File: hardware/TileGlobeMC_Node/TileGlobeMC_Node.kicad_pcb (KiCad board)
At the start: 2 copper layers, 85 x 40 mm, 164 parts, among them J1 P_Female, J10 LCD, J11 USB_C, J12 P_Female_Fallback, J13 P_Male_Fallback, J14 P_Female_Fallback, J15 P_Male_Fallback, J16 P_Female_Fallback, J17 P_Male_Fallback, J18 P_Female_Fallback, J19 P_Male_Fallback, J2 P_Male, J20 Conn_01x24_MountingPin, J21 Conn_01x24_MountingPin, J3 P_Female, J4 P_Male, J5 P_Female, J6 P_Male, J7 P_Female, J8 P_Male, J9 SWD, Q1 2N7002W, SW1 Left, SW2 Left, SW3 Left, SW4 Left, SW5 Left, U1 RP2350_80QFN, U2 TPS62A01PDDC, U3 BQ24232RGT, U4 ESP-PSRAM64H, U6 PY25Q128HA-SSH, U7 74AHC1G04, U8 LSM6DS3, U9 AW9523B, Y1 12M

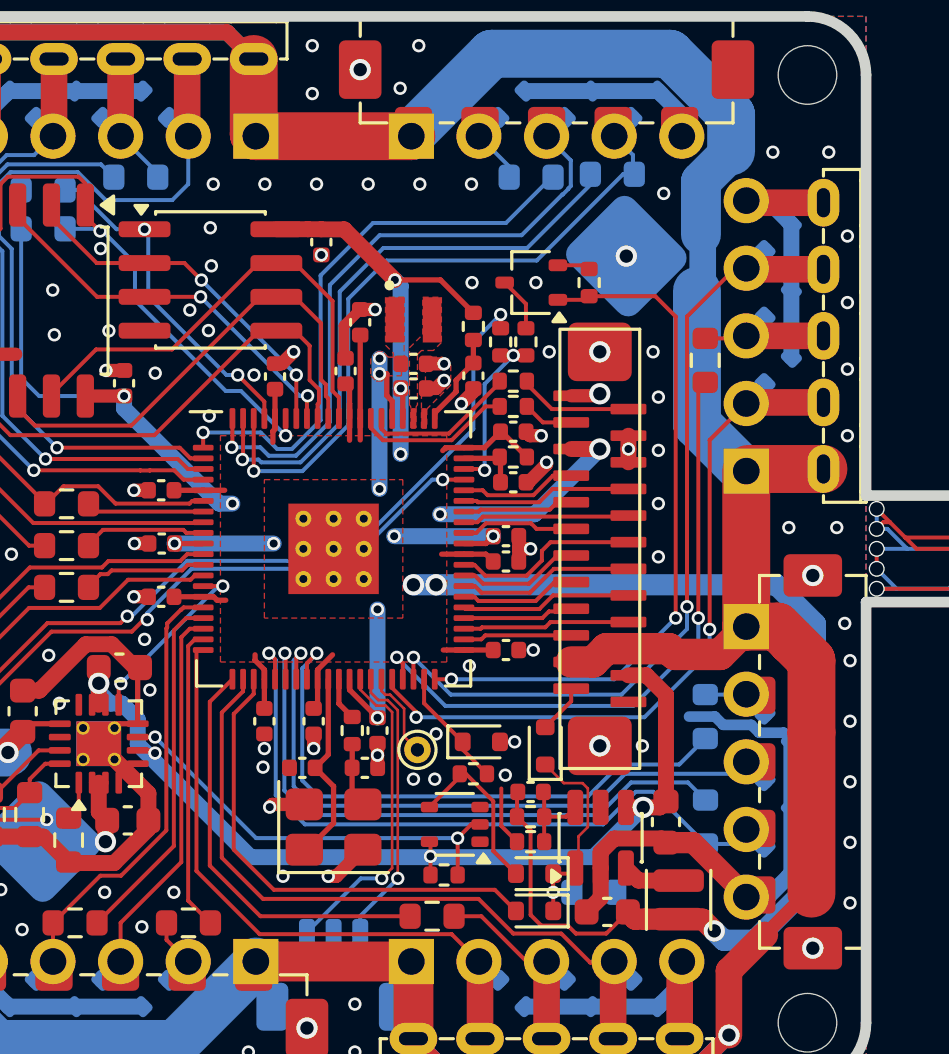
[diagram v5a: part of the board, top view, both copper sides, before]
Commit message: BOM; PCB minor tweaks
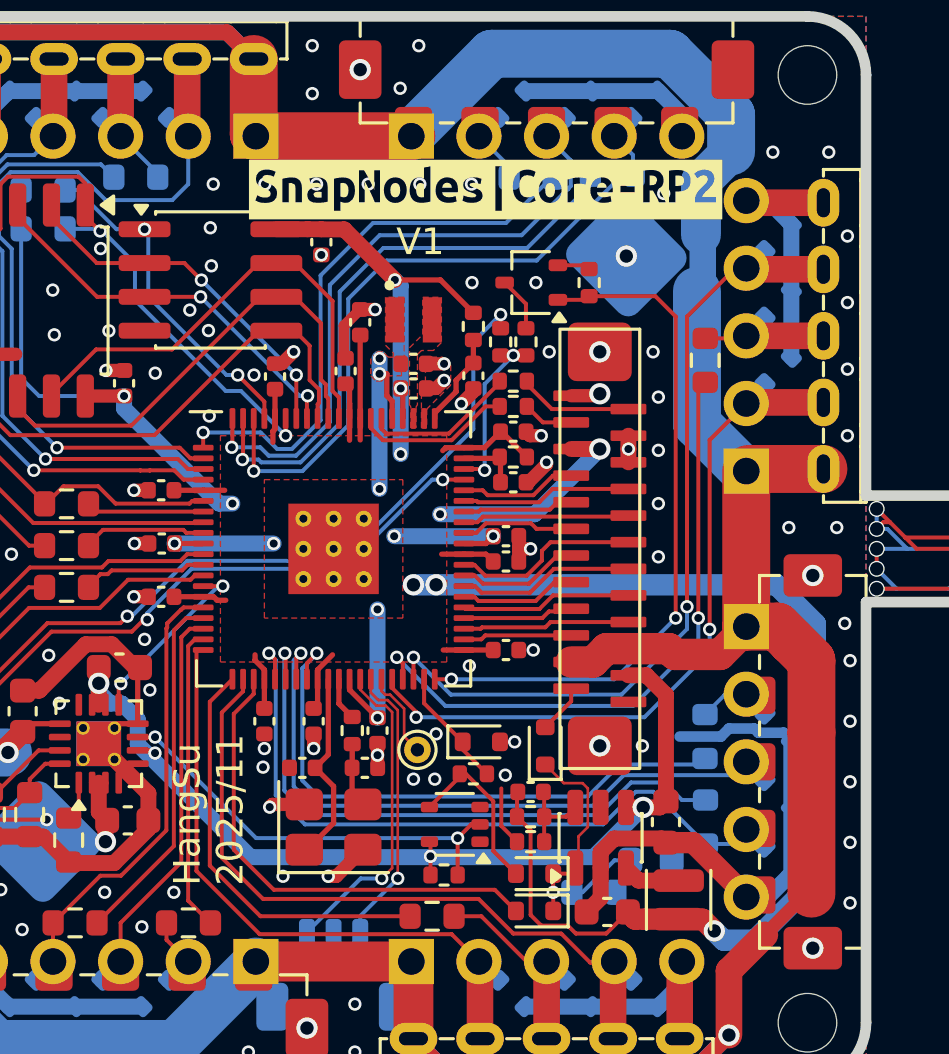
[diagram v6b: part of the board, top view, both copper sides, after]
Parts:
- added C37: 100n, Capacitor_SMD:C_0603_1608Metric, B.Cu at (11.9, 11.7)
- added kibuzzard-69136CB0: G***, kibuzzard-69136CB0, F.Cu at (5.71, -13.5)
- D10, D11, D12, D13, D14, D15, D16, D17, D18, D19, D20, D21, D22, D23, D24, D25, D26, D27, D28, D29, D6, D7, D8, D9: value ESD5Z3.3C -> ESD5Z3.3-HXY
- R17, R18: value 100k -> 10k
- moved R8 0.75 mm to (13.9, 7.05)
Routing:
- net Net-(D1-K): track 8.17 -> 10.9 mm
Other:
- board text added: "HangSu 2025/11"
- board text added: "V1"
